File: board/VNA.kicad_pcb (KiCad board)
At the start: 2 copper layers, 100 x 100 mm, 136 parts, among them J1 Conn_02x07_Odd_Even, J10 Conn_01x01, J11 Conn_01x01, J12 Conn_01x01, J13 Barrel_Jack, J15 Conn_02x05_Odd_Even, J17 Conn_01x04, J18 Conn_01x01, J19 Conn_01x01, J2 Conn_Coaxial, J20 Conn_01x01, J21 Conn_01x01, J22 Conn_01x02, J3 Conn_01x01, J4 Conn_01x01, J5 Conn_01x01, J6 Conn_01x01, J7 Conn_01x01, J8 Conn_01x01, J9 Conn_Coaxial, Q1 SS9018, U1 SI5351A, U2 LM339, U3 SA612, U4 SA612, U5 SA612, U6 LM358, U7 LM358, U8 LM1117-3.3, U9 LM7805_TO220, Y1 27 MHz

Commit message: Added JST 2.54 power and USB-B connecotrs
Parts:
- added J14: Conn_01x02, Connectors_Molex:Molex_KK-6410-02_02x2.54mm_Straight, F.Cu at (115.2, 146.6)
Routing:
- net Net-(C47-Pad1): track 53.0 -> 64.1 mm
- net DEMODCUR: track 177.2 -> 175.3 mm
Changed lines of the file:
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@@
 (kicad_pcb (version 4) (host pcbnew 4.0.7)
   (general
-    (links 262)
+    (links 264)
     (no_connects 0)
-    (area 48.252381 29.036639 153.343482 154.699701)
+    (area 49.924999 49.924999 150.075001 150.075001)
     (thickness 1.6)
-    (drawings 38)
-    (tracks 1659)
+    (drawings 40)
+    (tracks 1664)
     (zones 0)
-    (modules 136)
+    (modules 137)
     (nets 83)
   )
@@
   )
   (setup
-    (last_trace_width 0.25)
+    (last_trace_width 1)
     (user_trace_width 0.35)
     (user_trace_width 0.5)
@@
     )
   )
+  (module Connectors_Molex:Molex_KK-6410-02_02x2.54mm_Straight (layer F.Cu)
+    (at 115.2 146.6)
+    (descr "Connector Headers with Friction Lock, 22-27-2021, http://www.molex.com/pdm_docs/sd/022272021_sd.pdf")
+    (tags "connector molex kk_6410 22-27-2021")
+    (fp_text reference J14 (at -3.5 -2.6) (layer F.SilkS)
+      (effects (font (size 1 1) (thickness 0.15)))
+    )
+    (fp_text value Conn_01x02 (at 1.27 4.5) (layer F.Fab)
+      (effects (font (size 1 1) (thickness 0.15)))
+    )
+    (fp_line (start -1.47 -3.12) (end -1.47 3.08) (layer F.Fab) (width 0.12))
+    (fp_line (start -1.47 3.08) (end 4.01 3.08) (layer F.Fab) (width 0.12))
+    (fp_line (start 4.01 3.08) (end 4.01 -3.12) (layer F.Fab) (width 0.12))
+    (fp_line (start 4.01 -3.12) (end -1.47 -3.12) (layer F.Fab) (width 0.12))
+    (fp_line (start -1.37 -3.02) (end -1.37 2.98) (layer F.SilkS) (width 0.12))
+    (fp_line (start -1.37 2.98) (end 3.91 2.98) (layer F.SilkS) (width 0.12))
+    (fp_line (start 3.91 2.98) (end 3.91 -3.02) (layer F.SilkS) (width 0.12))
+    (fp_line (start 3.91 -3.02) (end -1.37 -3.02) (layer F.SilkS) (width 0.12))
+    (fp_line (start 0 2.98) (end 0 1.98) (layer F.SilkS) (width 0.12))
+    (fp_line (start 0 1.98) (end 2.54 1.98) (layer F.SilkS) (width 0.12))
+    (fp_line (start 2.54 1.98) (end 2.54 2.98) (layer F.SilkS) (width 0.12))
+    (fp_line (start 0 1.98) (end 0.25 1.55) (layer F.SilkS) (width 0.12))
+    (fp_line (start 0.25 1.55) (end 2.29 1.55) (layer F.SilkS) (width 0.12))
+    (fp_line (start 2.29 1.55) (end 2.54 1.98) (layer F.SilkS) (width 0.12))
+    (fp_line (start 0.25 2.98) (end 0.25 1.98) (layer F.SilkS) (width 0.12))
+    (fp_line (start 2.29 2.98) (end 2.29 1.98) (layer F.SilkS) (width 0.12))
+    (fp_line (start -0.8 -3.02) (end -0.8 -2.4) (layer F.SilkS) (width 0.12))
+    (fp_line (start -0.8 -2.4) (end 0.8 -2.4) (layer F.SilkS) (width 0.12))
+    (fp_line (start 0.8 -2.4) (end 0.8 -3.02) (layer F.SilkS) (width 0.12))
+    (fp_line (start 1.74 -3.02) (end 1.74 -2.4) (layer F.SilkS) (width 0.12))
+    (fp_line (start 1.74 -2.4) (end 3.34 -2.4) (layer F.SilkS) (width 0.12))
+    (fp_line (start 3.34 -2.4) (end 3.34 -3.02) (layer F.SilkS) (width 0.12))
+    (fp_line (start -1.9 3.5) (end -1.9 -3.55) (layer F.CrtYd) (width 0.05))
+    (fp_line (start -1.9 -3.55) (end 4.45 -3.55) (layer F.CrtYd) (width 0.05))
+    (fp_line (start 4.45 -3.55) (end 4.45 3.5) (layer F.CrtYd) (width 0.05))
+    (fp_line (start 4.45 3.5) (end -1.9 3.5) (layer F.CrtYd) (width 0.05))
+    (fp_text user %R (at 1.27 0) (layer F.Fab)
+      (effects (font (size 1 1) (thickness 0.15)))
+    )
+    (pad 1 thru_hole rect (at 0 0) (size 2 2.6) (drill 1.2) (layers *.Cu *.Mask)
+      (net 2 GND))
+    (pad 2 thru_hole oval (at 2.54 0) (size 2 2.6) (drill 1.2) (layers *.Cu *.Mask)
+      (net 53 "Net-(C47-Pad1)"))
+    (model ${KISYS3DMOD}/Connectors_Molex.3dshapes/Molex_KK-6410-02_02x2.54mm_Straight.wrl
+      (at (xyz 0 0 0))
+      (scale (xyz 1 1 1))
+      (rotate (xyz 0 0 0))
+    )
+  )
+  (gr_text +V (at 120.4 146.6 90) (layer F.SilkS)
+    (effects (font (size 1 1) (thickness 0.15)))
+  )
+  (gr_text GND (at 112.2 146.8 90) (layer F.SilkS)
+    (effects (font (size 1 1) (thickness 0.15)))
+  )
   (gr_text 1 (at 59 138.5) (layer F.SilkS)
     (effects (font (size 1 1) (thickness 0.15)))
@@
   (segment (start 128.49924 88.7584) (end 132.47624 88.7584) (width 0.35) (layer F.Cu) (net 34) (status 20))
   (segment (start 126.85014 87.1093) (end 128.49924 88.7584) (width 0.35) (layer F.Cu) (net 34))
+  (segment (start 120.5738 142.5) (end 120.5 142.5) (width 0.35) (layer B.Cu) (net 35))
+  (segment (start 113.75 144.75) (end 110.3933 148.8567) (width 0.35) (layer B.Cu) (net 35))
+  (segment (start 117.25 144.75) (end 113.75 144.75) (width 0.35) (layer B.Cu) (net 35))
+  (segment (start 120.5 142.5) (end 117.25 144.75) (width 0.35) (layer B.Cu) (net 35))
   (segment (start 129.3495 128.3589) (end 129.3495 128.5113) (width 0.35) (layer B.Cu) (net 35))
   (segment (start 129.3495 128.5113) (end 120.5738 137.287) (width 0.35) (layer B.Cu) (net 35))
   (segment (start 143.4211 98.7044) (end 142.53464 98.7044) (width 0.35) (layer F.Cu) (net 35))
-  (segment (start 120.5738 137.287) (end 120.5738 145.7452) (width 0.35) (layer B.Cu) (net 35))
+  (segment (start 120.5738 137.287) (end 120.5738 142.5) (width 0.35) (layer B.Cu) (net 35))
   (segment (start 82.6643 146.1643) (end 80.264 143.764) (width 0.35) (layer B.Cu) (net 35) (status 20))
   (segment (start 82.6643 147.9677) (end 82.6643 146.1643) (width 0.35) (layer B.Cu) (net 35))
   (segment (start 83.5533 148.8567) (end 82.6643 147.9677) (width 0.35) (layer B.Cu) (net 35))
-  (segment (start 117.4623 148.8567) (end 83.5533 148.8567) (width 0.35) (layer B.Cu) (net 35))
-  (segment (start 120.5738 145.7452) (end 117.4623 148.8567) (width 0.35) (layer B.Cu) (net 35))
+  (segment (start 110.3933 148.8567) (end 83.5533 148.8567) (width 0.35) (layer B.Cu) (net 35))
   (segment (start 144.3228 129.0447) (end 144.3228 128.9685) (width 0.35) (layer B.Cu) (net 35))
   (segment (start 140.2588 129.0447) (end 144.3228 129.0447) (width 0.35) (layer B.Cu) (net 35))
@@
   (segment (start 71.07936 115.3033) (end 71.07936 115.71798) (width 0.25) (layer F.Cu) (net 52) (status 30))
   (segment (start 76.032 112.268) (end 75.271741 112.252701) (width 0.25) (layer F.Cu) (net 52) (status 10))
+  (segment (start 117.74 146.6) (end 120.1635 146.6) (width 1) (layer F.Cu) (net 53))
+  (segment (start 120.1635 146.6) (end 126.2888 140.4747) (width 1) (layer F.Cu) (net 53))
   (segment (start 145.6436 116.7384) (end 145.1102 116.7384) (width 0.5) (layer F.Cu) (net 53) (status 30))
   (segment (start 145.1102 116.7384) (end 143.764 118.6688) (width 0.5) (layer F.Cu) (net 53) (status 10))

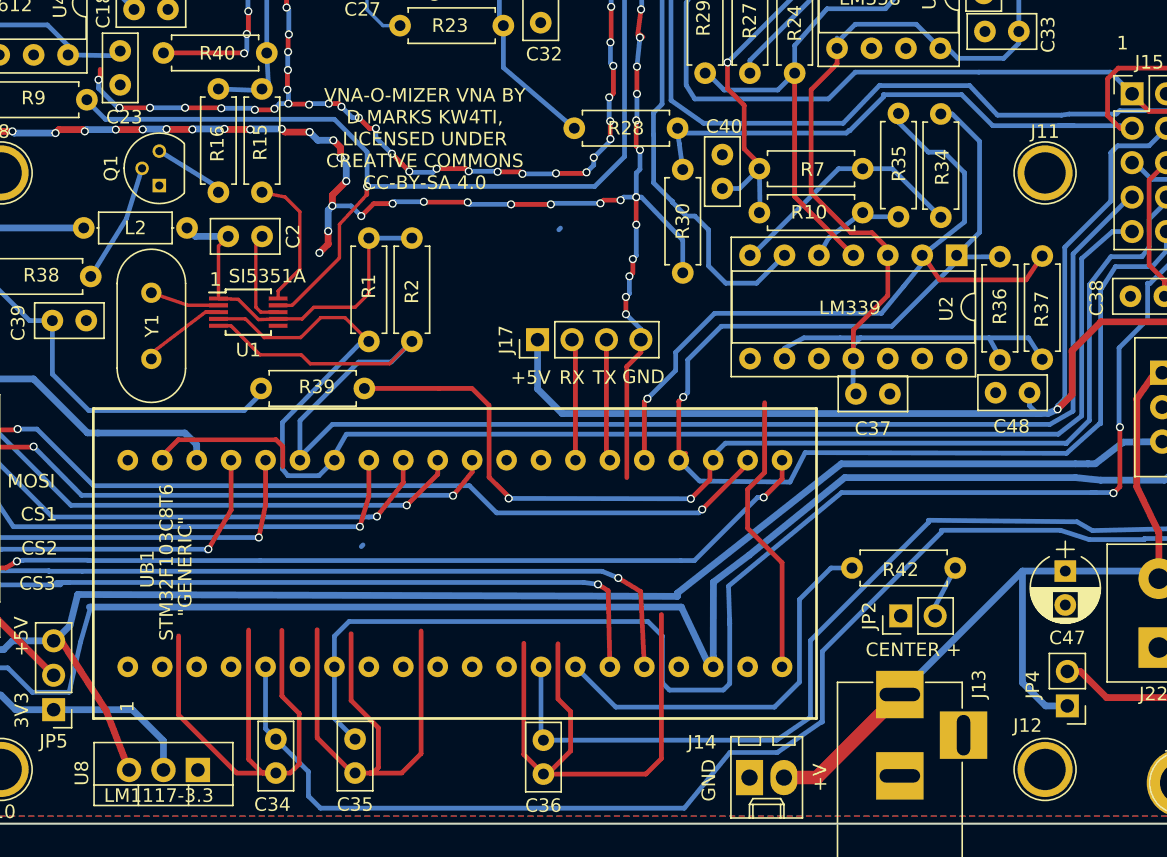
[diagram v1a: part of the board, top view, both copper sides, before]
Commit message: Changes to finalize two SI5351A solution
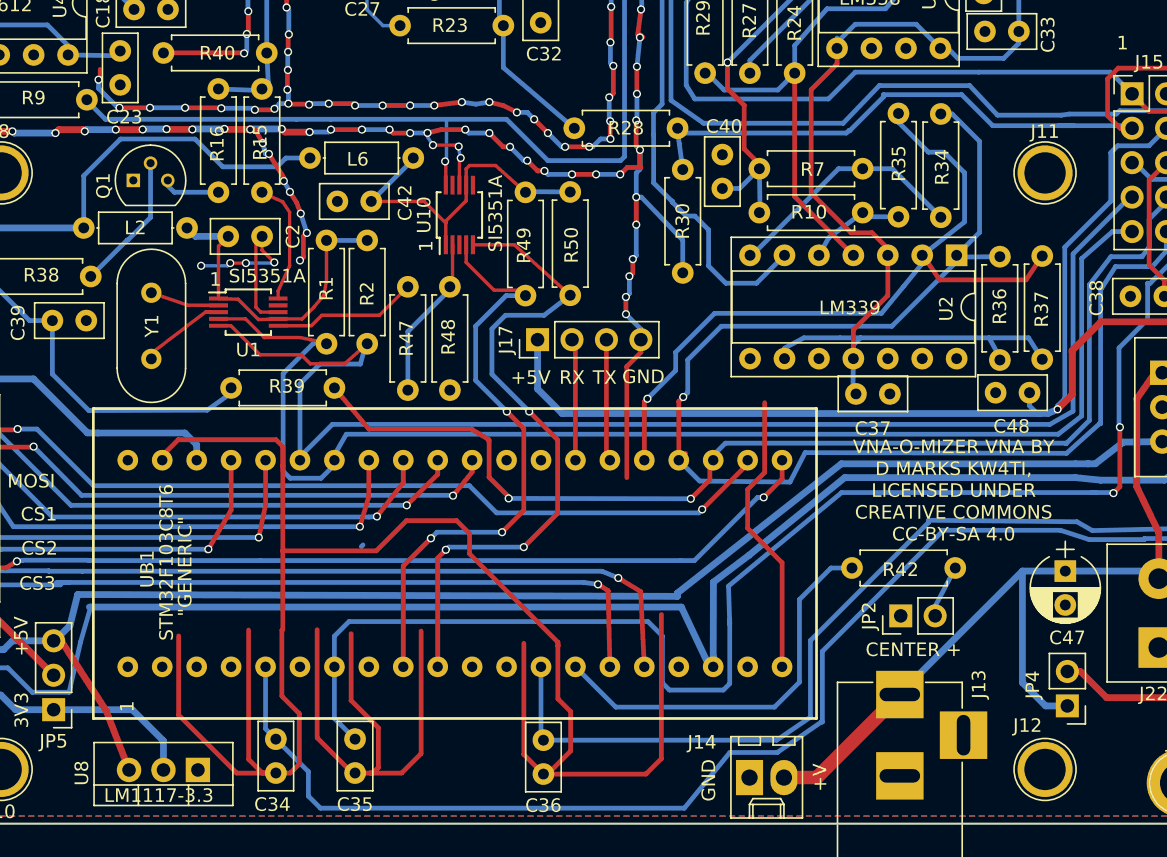
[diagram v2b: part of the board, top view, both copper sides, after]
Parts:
- added C42: 100 nF, Capacitors_THT:C_Disc_D5.0mm_W2.5mm_P2.50mm, F.Cu at (84.8, 104.1)
- added L6: Ferrite_Bead_Small, Inductors_THT:L_Axial_L5.3mm_D2.2mm_P7.62mm_Horizontal_Vishay_IM-1, F.Cu at (90.4, 100.9)
- added R47: 220R, Resistors_THT:R_Axial_DIN0207_L6.3mm_D2.5mm_P7.62mm_Horizontal, F.Cu at (90.0, 110.4)
- added R48: 100R, Resistors_THT:R_Axial_DIN0207_L6.3mm_D2.5mm_P7.62mm_Horizontal, F.Cu at (93.1, 110.4)
- added R49: 10k, Resistors_THT:R_Axial_DIN0207_L6.3mm_D2.5mm_P7.62mm_Horizontal, F.Cu at (98.7, 111.0)
- added R50: 10k, Resistors_THT:R_Axial_DIN0207_L6.3mm_D2.5mm_P7.62mm_Horizontal, F.Cu at (102.0, 111.0)
- added U10: SI5351A, Housings_SSOP:MSOP-10_3x3mm_Pitch0.5mm, F.Cu at (93.8, 105.1)
- moved R2 3.30 mm to (87.0, 114.6)
- moved R1 3.13 mm to (84.0, 114.6)
- moved R39 2.21 mm to (77.0, 117.9)
- moved Q1 1.95 mm to (69.8, 102.5), turned to 0 degrees
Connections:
- U1 pad 6: (no net) -> Net-(R47-Pad1)
- U1 pad 9: Net-(R43-Pad2) -> (no net)
- UB1 pad 14: (no net) -> SCL2
- UB1 pad 15: (no net) -> SDA2
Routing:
- net GND: track 700.8 -> 754.1 mm, vias 217 -> 229
- net SDA2: track 0.00 -> 49.2 mm, vias 0 -> 3
- net SCL2: track 0.00 -> 44.4 mm, vias 0 -> 3
- net Net-(C42-Pad2): track 0.00 -> 25.4 mm
- net +3V3: track 181.1 -> 203.8 mm
- net Net-(R47-Pad2): track 0.00 -> 12.1 mm
- net Net-(R47-Pad1): track 0.00 -> 10.8 mm
- net Net-(R43-Pad2): track 97.8 -> 87.6 mm
- net SDA: track 105.9 -> 101.2 mm
- net SCL: track 102.9 -> 98.3 mm
- net Net-(C2-Pad2): track 28.4 -> 24.9 mm
- net Net-(C39-Pad1): track 27.6 -> 25.3 mm
- net Net-(Q1-Pad2): track 8.90 -> 10.2 mm
- net Net-(R15-Pad2): track 10.3 -> 9.16 mm
- net Net-(Q1-Pad3): track 5.38 -> 4.33 mm
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
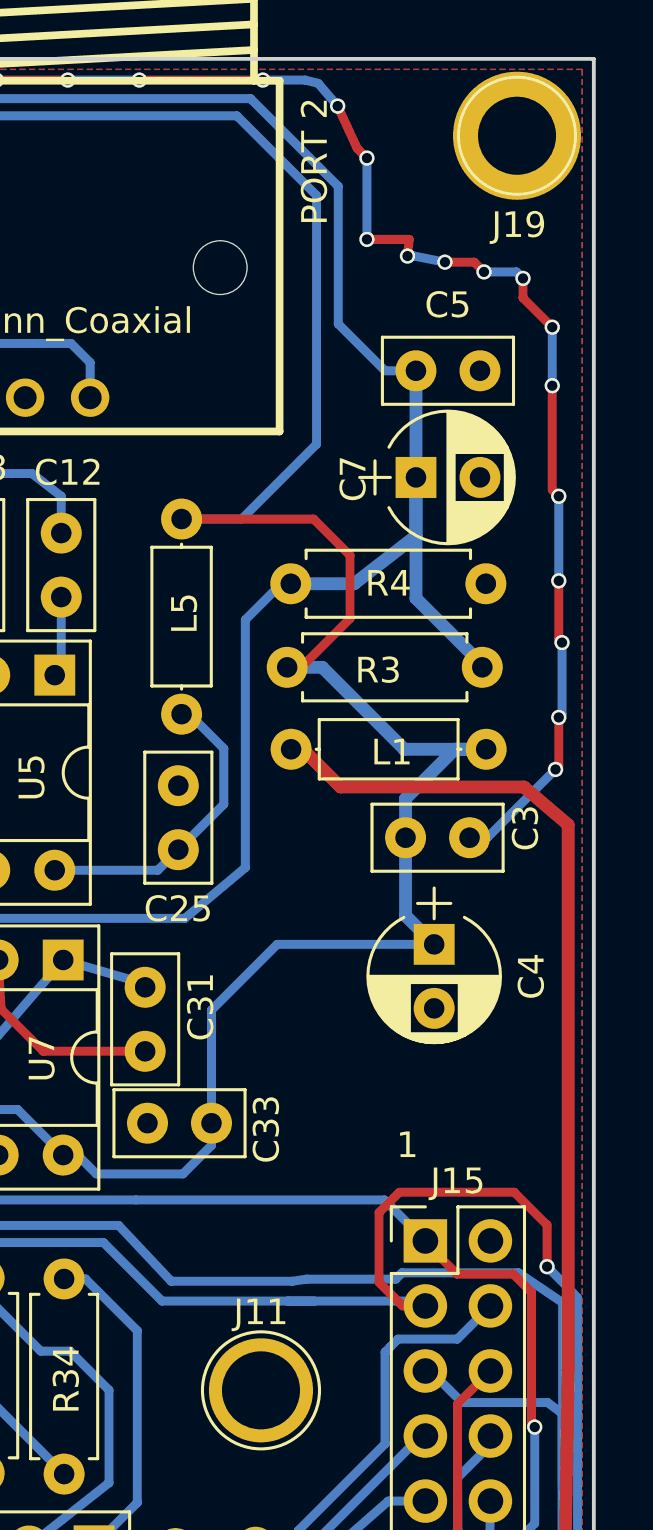
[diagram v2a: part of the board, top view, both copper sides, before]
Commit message: Updated software to add cursor for smith chart, also changed edge of triggering
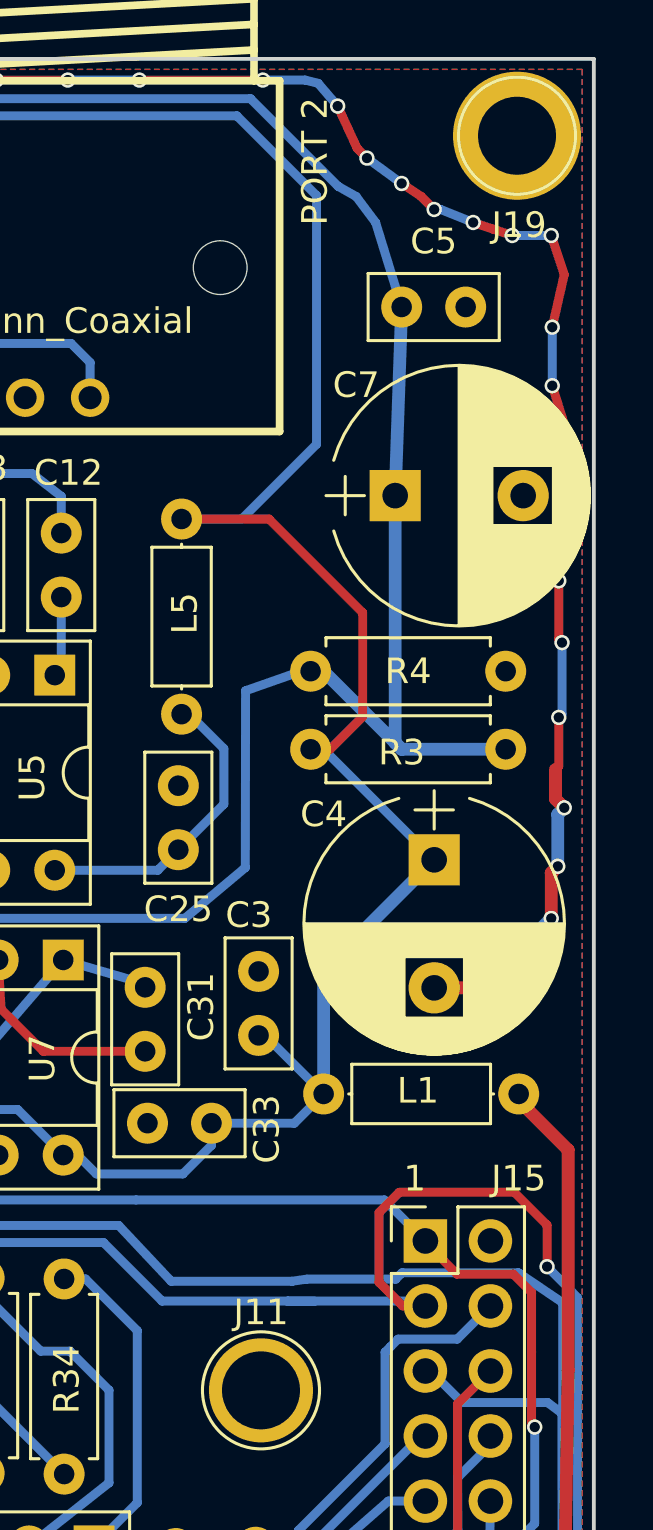
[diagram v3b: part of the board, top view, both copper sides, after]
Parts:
- C4: value 100 uF -> 1000 uF; footprint Capacitors_THT:CP_Radial_D5.0mm_P2.50mm -> Capacitors_THT:CP_Radial_D10.0mm_P5.00mm
- C7: value 10 uF -> 1000 uF; footprint Capacitors_THT:CP_Radial_D5.0mm_P2.50mm -> Capacitors_THT:CP_Radial_D10.0mm_P5.00mm
- R36, R37: value 1k -> 10k
- moved L1 14.9 mm to (139.4, 90.4), turned to 0 degrees
- moved C3 9.62 mm to (136.9, 88.1), turned to 90 degrees
- moved R4 3.50 mm to (138.9, 73.9)
- moved R3 3.33 mm to (138.9, 77.0)
- moved C4 3.30 mm to (143.8, 81.3)
- moved C5 2.55 mm to (142.5, 59.7)
- moved C7 1.08 mm to (142.2, 67.1)
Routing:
- net +5V: track 328.6 -> 306.9 mm
- net GND: track 754.1 -> 760.9 mm, vias 229 -> 232
- net FILT5V: track 310.5 -> 305.9 mm
